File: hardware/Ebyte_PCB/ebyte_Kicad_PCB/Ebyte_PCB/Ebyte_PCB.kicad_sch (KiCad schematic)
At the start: 30 parts, among them Q1 NPN, Q2 PMOS, U1 DF11, U2 LT8612IUDE, U3 E32-400M33S SX1278, U4 MIC69303RT, U5 CONMMCX001, U6 SN74LVC1G08DBVR

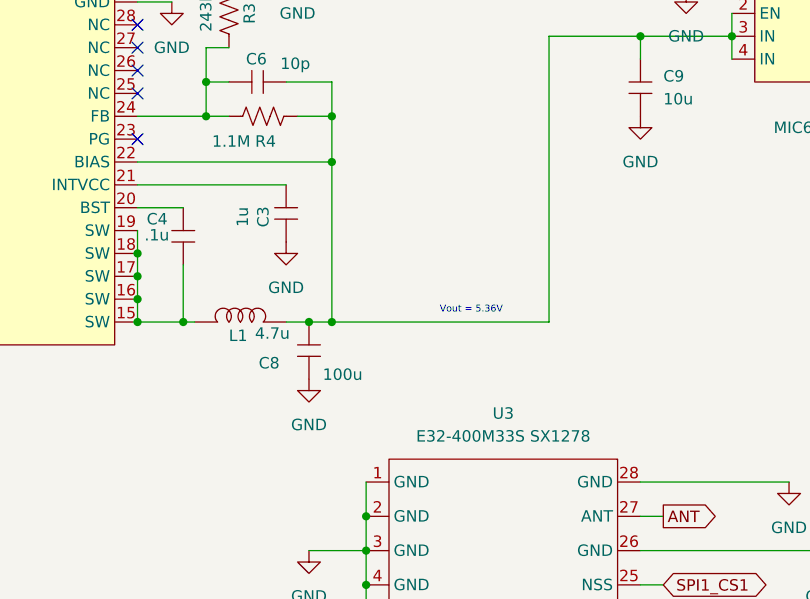
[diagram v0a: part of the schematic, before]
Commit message: Layout v2
added courtyards, grouped components per datasheet specs. unsure of load switch placement. still figuring out ldo 150u cap.
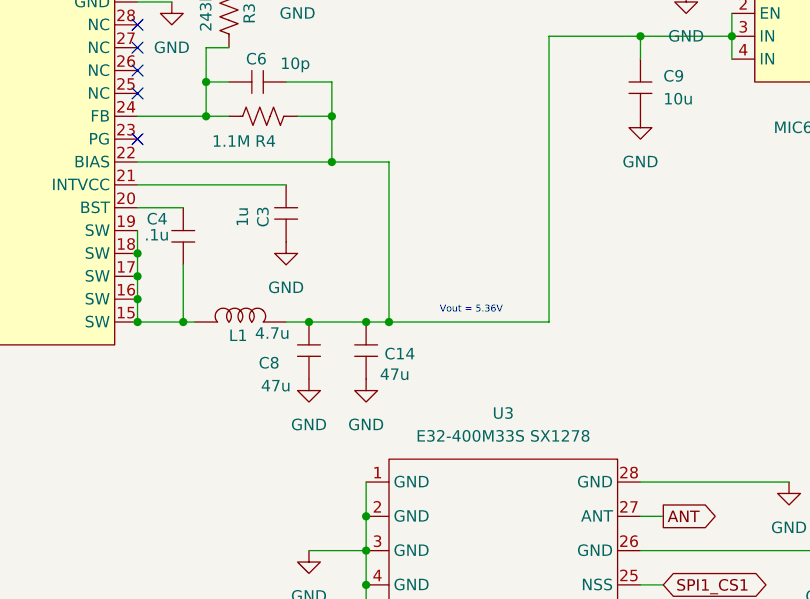
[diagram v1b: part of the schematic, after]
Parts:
- added C14: 47u, ebyte_footprints:C1210, symbol ebyte__symbols:Capacitor
- C13: footprint ebyte_footprints:CAP-SMD_L7.3-W4.3-R-RD -> Capacitor_Tantalum_SMD:CP_EIA-7343-31_Kemet-D
- C8: value 100u -> 47u; footprint ebyte_footprints:CAP-SMD_L7.3-W4.3-R-RD -> ebyte_footprints:C1210
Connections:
- net GND: now also C14.1
- net at C6.2, C8.2, C9.2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: now also C14.2
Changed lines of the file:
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@@
 	)
 	(junction
+		(at 114.3 121.92)
+		(diameter 0)
+		(color 0 0 0 0)
+	)
+	(junction
 		(at 114.3 147.32)
 		(diameter 0)
@@
 	)
 	(junction
-		(at 110.49 121.92)
+		(at 116.84 121.92)
 		(diameter 0)
 		(color 0 0 0 0)
@@
 	(wire
 		(pts
-			(xy 110.49 121.92) (xy 134.62 121.92)
+			(xy 116.84 121.92) (xy 134.62 121.92)
 		)
 		(stroke
@@
 	(wire
 		(pts
+			(xy 116.84 104.14) (xy 110.49 104.14)
+		)
+		(stroke
+			(width 0)
+			(type default)
+		)
+	)
+	(wire
+		(pts
 			(xy 60.96 88.9) (xy 60.96 85.09)
 		)
@@
 	(wire
 		(pts
+			(xy 114.3 121.92) (xy 107.95 121.92)
+		)
+		(stroke
+			(width 0)
+			(type default)
+		)
+	)
+	(wire
+		(pts
 			(xy 105.41 95.25) (xy 110.49 95.25)
 		)
@@
 	(wire
 		(pts
-			(xy 110.49 104.14) (xy 110.49 121.92)
+			(xy 116.84 104.14) (xy 116.84 121.92)
 		)
 		(stroke
@@
 	(wire
 		(pts
-			(xy 110.49 121.92) (xy 107.95 121.92)
+			(xy 116.84 121.92) (xy 114.3 121.92)
 		)
 		(stroke
@@
 	(symbol
 		(lib_id "power:GND")
+		(at 114.3 128.27 0)
+		(unit 1)
+		(exclude_from_sim no)
+		(in_bom yes)
+		(on_board yes)
+		(dnp no)
+		(fields_autoplaced yes)
+		(property "Reference" "#PWR031"
+			(at 114.3 134.62 0)
+			(effects
+				(font
+					(size 1.27 1.27)
+				)
+				(hide yes)
+			)
+		)
+		(property "Value" "GND"
+			(at 114.3 133.35 0)
+			(effects
+				(font
+					(size 1.27 1.27)
+				)
+			)
+		)
+		(property "Footprint" ""
+			(at 114.3 128.27 0)
+			(effects
+				(font
+					(size 1.27 1.27)
+				)
+				(hide yes)
+			)
+		)
+		(property "Datasheet" ""
+			(at 114.3 128.27 0)
+			(effects
+				(font
+					(size 1.27 1.27)
+				)
+				(hide yes)
+			)
+		)
+		(property "Description" "Power symbol creates a global label with name \"GND\" , ground"
+			(at 114.3 128.27 0)
+			(effects
+				(font
+					(size 1.27 1.27)
+				)
+				(hide yes)
+			)
+		)
+		(pin "1"
+		)
+		(instances
+			(project "Ebyte_PCB"
+				(path "/f654da80-73c6-440d-a1fb-60b191de58e0"
+					(reference "#PWR031")
+					(unit 1)
+				)
+			)
+		)
+	)
+	(symbol
+		(lib_id "power:GND")
 		(at 38.1 101.6 0)
 		(unit 1)
@@
 			)
 		)
-		(property "Value" "100u"
-			(at 109.474 127.762 90)
+		(property "Value" "47u"
+			(at 102.616 129.032 90)
 			(effects
 				(font
@@
 			)
 		)
-		(property "Footprint" "ebyte_footprints:CAP-SMD_L7.3-W4.3-R-RD"
+		(property "Footprint" "ebyte_footprints:C1210"
 			(at 107.95 124.46 0)
 			(effects
@@
 			)
 		)
-		(property "Footprint" "ebyte_footprints:CAP-SMD_L7.3-W4.3-R-RD"
+		(property "Footprint" "Capacitor_Tantalum_SMD:CP_EIA-7343-31_Kemet-D"
 			(at 219.71 92.71 0)
 			(effects
@@
 					(unit 1)
 				)
+			)
+		)
+	)
+	(symbol
+		(lib_id "ebyte__symbols:Capacitor")
+		(at 114.3 124.46 90)
+		(unit 1)
+		(exclude_from_sim no)
+		(in_bom yes)
+		(on_board yes)
+		(dnp no)
+		(property "Reference" "C14"
+			(at 116.332 125.476 90)
+			(effects
+				(font
+					(size 1.27 1.27)
+				)
+				(justify right)
+			)
+		)
+		(property "Value" "47u"
+			(at 115.824 127.762 90)
+			(effects
+				(font
+					(size 1.27 1.27)
+				)
+				(justify right)
+			)
+		)
+		(property "Footprint" "ebyte_footprints:C1210"
+			(at 114.3 124.46 0)
+			(effects
+				(font
+					(size 1.27 1.27)
+				)
+				(hide yes)
+			)
+		)
+		(property "Datasheet" ""
+			(at 114.3 124.46 0)
+			(effects
+				(font
+					(size 1.27 1.27)
+				)
+				(hide yes)
+			)
+		)
+		(property "Description" ""
+			(at 114.3 124.46 0)
+			(effects
+				(font
+					(size 1.27 1.27)
+				)
+				(hide yes)
+			)
+		)
+		(pin "1"
+		)
+		(pin "2"
+		)
+		(instances
+			(project "Ebyte_PCB"
+				(path "/f654da80-73c6-440d-a1fb-60b191de58e0"
+					(reference "C14")
+					(unit 1)
+				)
